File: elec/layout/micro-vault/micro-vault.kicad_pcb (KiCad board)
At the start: 2 copper layers, 2 parts

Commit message: layout complete
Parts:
- added C1: 100nF ±10% 16V X7R, atopile:C0402-b3ef17, F.Cu at (111.5, 89.5)
- added C2: 10µF ±10% 10V X5R, atopile:C0603-bd72f6, F.Cu at (114.7, 95.0)
- added C3: 100nF ±10% 16V X7R, atopile:C0402-b3ef17, F.Cu at (107.9, 94.6)
- added C4: 1µF ±10% 25V X5R, atopile:C0402-b3ef17, F.Cu at (116.4, 94.8)
- added C5: 1µF ±10% 25V X5R, atopile:C0402-b3ef17, F.Cu at (124.0, 93.5)
- added C6: 10µF ±10% 10V X5R, atopile:C0603-bd72f6, F.Cu at (124.2, 94.8)
- added C7: 10µF ±10% 10V X5R, atopile:C0603-bd72f6, F.Cu at (124.2, 96.2)
- added C8: 1µF ±10% 25V X5R, atopile:C0402-b3ef17, F.Cu at (113.5, 108.1)
- added C9: 1µF ±10% 25V X5R, atopile:C0402-b3ef17, F.Cu at (109.1, 108.1)
- added Q1: , atopile:SOT-23-3_L2.9-W1.6-P1.90-LS2.8-BR-186170, F.Cu at (123.9, 100.1)
- added R1: 1MΩ ±1% 62.5mW, atopile:R0402-56259e, F.Cu at (119.1, 107.0)
- added R10: 3kΩ ±0% 62.5mW, atopile:R0402-56259e, F.Cu at (112.3, 105.8)
- added R11: 10kΩ ±1% 62.5mW, atopile:R0402-56259e, F.Cu at (110.3, 105.8)
- added R12: 22Ω ±1% 100mW, atopile:R0603-ebcab9, F.Cu at (120.0, 90.2)
- added R13: 22Ω ±1% 100mW, atopile:R0603-ebcab9, F.Cu at (115.6, 92.0)
- added R14: 22Ω ±1% 100mW, atopile:R0603-ebcab9, F.Cu at (107.6, 91.7)
- added R15: 22Ω ±1% 100mW, atopile:R0603-ebcab9, F.Cu at (111.3, 100.4)
- added R2: 22Ω ±1% 100mW, atopile:R0603-ebcab9, F.Cu at (115.7, 97.5)
- added R3: 22Ω ±1% 100mW, atopile:R0603-ebcab9, F.Cu at (119.9, 99.4)
- added R4: 22Ω ±1% 100mW, atopile:R0603-ebcab9, F.Cu at (123.9, 97.8)
- added R5: 22Ω ±1% 100mW, atopile:R0603-ebcab9, F.Cu at (123.6, 92.2)
- added R6: 10kΩ ±1% 62.5mW, atopile:R0402-56259e, F.Cu at (126.5, 100.3)
- added R7: 10kΩ ±1% 62.5mW, atopile:R0402-56259e, F.Cu at (126.5, 98.2)
- added R8: 12kΩ ±1% 62.5mW, atopile:R0402-56259e, F.Cu at (122.6, 109.7)
- added R9: 88.7kΩ ±0% 62.5mW, atopile:R0402-56259e, F.Cu at (120.6, 109.7)
- added U3: , atopile:TSSOP-16_L5.0-W4.4-P0.65-LS6.4-BL-4f6acc, F.Cu at (111.2, 94.6)
- added U5: , atopile:VSSOP-8_L3.0-W3.0-P0.65-LS4.9-BL-beff67, F.Cu at (122.7, 107.4)
- added U6: , atopile:SOIC-8_L5.0-W4.0-P1.27-LS6.0-BL-294f77, F.Cu at (119.8, 94.7)
- added U7: , lib:SOT-23-5_L3.0-W1.7-P0.95-LS2.8-BL, F.Cu at (111.2, 108.3)
- added U8: , atopile:WSON-6_L2.0-W2.0-P0.65-TL-EP-c93430, F.Cu at (115.5, 99.9)
- U1: footprint atopile:TSSOP-16_L5.0-W4.4-P0.65-LS6.4-BL-4f6acc -> lib:NetTie-2_SMD_Pad0.25mm
- U2: footprint atopile:SOIC-8_L5.0-W4.0-P1.27-LS6.0-BL-294f77 -> lib:NetTie-2_SMD_Pad0.25mm
- moved U2 151.9 mm to (111.6, 93.0), turned to 180 degrees
- moved U1 146.4 mm to (110.5, 96.0)
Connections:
- U1 pad 1: A0 -> gnd
- U1 pad 2: A1 -> gnd-1
- U2 pad 1: DNC -> hv-2
- U2 pad 2: VIN -> hv-1
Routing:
- net gnd: track 0.00 -> 91.3 mm, vias 0 -> 7
- net hv-1: track 0.00 -> 51.8 mm, vias 0 -> 6
- net SCL: track 0.00 -> 21.2 mm, vias 0 -> 2
- net hv-3: track 0.00 -> 20.5 mm, vias 0 -> 2
- net SDA: track 0.00 -> 19.5 mm, vias 0 -> 2
- net Vplus: track 0.00 -> 17.5 mm, vias 0 -> 2
- net OUT1: track 0.00 -> 16.8 mm
- net TEMP: track 0.00 -> 16.5 mm, vias 0 -> 2
- net gnd-1: track 0.00 -> 15.1 mm, vias 0 -> 3
- net heater_controller-gnd: track 0.00 -> 12.6 mm, vias 0 -> 2
- net heater_controller-net-5: track 0.00 -> 10.5 mm, vias 0 -> 2
- net heater_controller-net-6: track 0.00 -> 9.44 mm
- net hv-2: track 0.00 -> 7.33 mm, vias 0 -> 2
- net heater_controller-net-4: track 0.00 -> 7.27 mm
- net hv: track 0.00 -> 7.05 mm
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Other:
- board outline added: 28 x 20 mm

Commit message: add logo
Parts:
- R10: value 3kΩ ±0% 62.5mW -> 10kΩ ±1% 62.5mW
- R11: value 10kΩ ±1% 62.5mW -> 36kΩ ±1% 62.5mW
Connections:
- C3 pad 1: hv-1 -> hv-3
- C4 pad 1: hv-1 -> hv-3
- C8 pad 1: hv-3 -> hv-1
- C9 pad 1: hv-1 -> hv-3
- R11 pad 1: hv-1 -> hv-3
- R12 pad 1: heater_controller-net-3 -> heater_controller-net-1
- R12 pad 2: heater_controller-net-1 -> heater_controller-net
- R13 pad 1: heater_controller-net-1 -> heater_controller-net
- R13 pad 2: heater_controller-net-5 -> heater_controller-net-4
- R14 pad 1: heater_controller-net-5 -> heater_controller-net-4
- R14 pad 2: heater_controller-net-6 -> heater_controller-net-2
- R15 pad 1: heater_controller-net-6 -> heater_controller-net-2
- R2 pad 1: hv-3 -> hv-1
- R2 pad 2: heater_controller-net -> heater_controller-net-3
- R3 pad 1: heater_controller-net -> heater_controller-net-3
- R3 pad 2: heater_controller-net-2 -> heater_controller-net-6
- R4 pad 1: heater_controller-net-2 -> heater_controller-net-6
- R4 pad 2: heater_controller-net-4 -> heater_controller-net-5
- R5 pad 1: heater_controller-net-4 -> heater_controller-net-5
- R5 pad 2: heater_controller-net-3 -> heater_controller-net-1
- R9 pad 1: hv-1 -> hv-3
- U2 pad 2: hv-1 -> hv-3
- U3 pad 13: hv-1 -> hv-3
- U3 pad 3: hv-1 -> hv-3
- U6 pad 2: hv-1 -> hv-3
- U7 pad 1: hv-3 -> hv-1
- U7 pad 3: hv-3 -> hv-1
- U7 pad 5: hv-1 -> hv-3
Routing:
- net hv-3: track 20.5 -> 51.8 mm, vias 2 -> 6
- net hv-1: track 51.8 -> 20.5 mm, vias 6 -> 2
- net heater_controller-net-6: track 9.44 -> 2.93 mm
- net heater_controller-net-2: track 2.93 -> 9.44 mm
- net heater_controller-net-5: track 10.5 -> 7.27 mm, vias 2 -> 0
- net heater_controller-net-4: track 7.27 -> 10.5 mm, vias 0 -> 2

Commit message: update layout
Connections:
- net TEMP renamed IN1minus
- C3 pad 1: hv-3 -> hv-1
- C4 pad 1: hv-3 -> hv-1
- C8 pad 1: hv-1 -> hv-3
- C9 pad 1: hv-3 -> hv-1
- R11 pad 1: hv-3 -> hv-1
- R12 pad 1: heater_controller-net-1 -> heater_controller-net-5
- R13 pad 2: heater_controller-net-4 -> heater_controller-net-1
- R14 pad 1: heater_controller-net-4 -> heater_controller-net-1
- R14 pad 2: heater_controller-net-2 -> heater_controller-net-4
- R15 pad 1: heater_controller-net-2 -> heater_controller-net-4
- R2 pad 1: hv-1 -> hv-3
- R2 pad 2: heater_controller-net-3 -> heater_controller-net-2
- R3 pad 1: heater_controller-net-3 -> heater_controller-net-2
- R4 pad 2: heater_controller-net-5 -> heater_controller-net-3
- R5 pad 1: heater_controller-net-5 -> heater_controller-net-3
- R5 pad 2: heater_controller-net-1 -> heater_controller-net-5
- R9 pad 1: hv-3 -> hv-1
- U2 pad 2: hv-3 -> hv-1
- U3 pad 13: hv-3 -> hv-1
- U3 pad 3: hv-3 -> hv-1
- U6 pad 2: hv-3 -> hv-1
- U7 pad 1: hv-1 -> hv-3
- U7 pad 3: hv-1 -> hv-3
- U7 pad 5: hv-3 -> hv-1
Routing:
- net hv-3: track 51.8 -> 20.5 mm, vias 6 -> 2
- net hv-1: track 20.5 -> 51.8 mm, vias 2 -> 6
- net heater_controller-net-1: track 3.89 -> 10.5 mm, vias 0 -> 2
- net heater_controller-net-2: track 9.44 -> 3.53 mm
- net heater_controller-net-3: track 3.53 -> 7.27 mm
- net heater_controller-net-5: track 7.27 -> 3.89 mm
- net heater_controller-net-4: track 10.5 -> 9.44 mm, vias 2 -> 0
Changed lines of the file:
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@@
 	(net 4 "IN2minus")
 	(net 5 "hv-2")
-	(net 6 "heater_controller-net-3")
+	(net 6 "heater_controller-net-2")
 	(net 7 "gnd")
 	(net 8 "reference.ic.footprint.pins[6].net-net")
@@
 	(net 17 "TRIMNR")
 	(net 18 "ADJ_NC")
-	(net 19 "heater_controller-net-5")
+	(net 19 "heater_controller-net-3")
 	(net 20 "AIN1")
 	(net 21 "IN2plus")
-	(net 22 "hv-3")
+	(net 22 "hv-1")
 	(net 23 "heater_controller-net-6")
 	(net 24 "REFN")
 	(net 25 "SCL")
-	(net 26 "TEMP")
-	(net 27 "hv-1")
+	(net 26 "IN1minus")
+	(net 27 "hv-3")
 	(net 28 "IN1plus")
 	(net 29 "gate")
 	(net 30 "heater_controller-gnd")
-	(net 31 "heater_controller-net-4")
-	(net 32 "heater_controller-net-2")
-	(net 33 "heater_controller-net-1")
+	(net 31 "heater_controller-net-1")
+	(net 32 "heater_controller-net-4")
+	(net 33 "heater_controller-net-5")
 	(net 34 "heater_controller-net")
 	(net 35 "OUT1")
@@
 			(size 0.81 0.86)
 			(layers "F.Cu" "F.Mask" "F.Paste")
-			(net 31 "heater_controller-net-4")
+			(net 31 "heater_controller-net-1")
 		)
 		(embedded_fonts no)
@@
 			(size 0.79 0.54)
 			(layers "F.Cu" "F.Mask" "F.Paste")
-			(net 22 "hv-3")
+			(net 22 "hv-1")
 		)
 		(pad "2" smd rect
@@
 			(size 0.81 0.86)
 			(layers "F.Cu" "F.Mask" "F.Paste")
-			(net 27 "hv-1")
+			(net 27 "hv-3")
 		)
 		(pad "2" smd rect
@@
 			(size 0.81 0.86)
 			(layers "F.Cu" "F.Mask" "F.Paste")
-			(net 6 "heater_controller-net-3")
+			(net 6 "heater_controller-net-2")
 		)
 		(embedded_fonts no)
@@
 			(size 0.81 0.86)
 			(layers "F.Cu" "F.Mask" "F.Paste")
-			(net 19 "heater_controller-net-5")
+			(net 19 "heater_controller-net-3")
 		)
 		(pad "2" smd rect
@@
 			(size 0.81 0.86)
 			(layers "F.Cu" "F.Mask" "F.Paste")
-			(net 33 "heater_controller-net-1")
+			(net 33 "heater_controller-net-5")
 		)
 		(embedded_fonts no)
@@
 			(size 0.25 0.25)
 			(layers "F.Cu")
-			(net 22 "hv-3")
+			(net 22 "hv-1")
 		)
 		(embedded_fonts no)
@@
 			(size 0.57 0.54)
 			(layers "F.Cu" "F.Mask" "F.Paste")
-			(net 22 "hv-3")
+			(net 22 "hv-1")
 		)
 		(pad "2" smd rect
@@
 			(size 0.79 0.54)
 			(layers "F.Cu" "F.Mask" "F.Paste")
-			(net 22 "hv-3")
+			(net 22 "hv-1")
 		)
 		(pad "2" smd rect
@@
 			(size 0.81 0.86)
 			(layers "F.Cu" "F.Mask" "F.Paste")
-			(net 32 "heater_controller-net-2")
+			(net 32 "heater_controller-net-4")
 		)
 		(pad "2" smd rect
@@
 			(size 0.79 0.54)
 			(layers "F.Cu" "F.Mask" "F.Paste")
-			(net 27 "hv-1")
+			(net 27 "hv-3")
 		)
 		(pad "2" smd rect
@@
 			(size 0.81 0.86)
 			(layers "F.Cu" "F.Mask" "F.Paste")
-			(net 6 "heater_controller-net-3")
+			(net 6 "heater_controller-net-2")
 		)
 		(pad "2" smd rect
@@
 			(size 0.57 0.54)
 			(layers "F.Cu" "F.Mask" "F.Paste")
-			(net 22 "hv-3")
+			(net 22 "hv-1")
 		)
 		(pad "2" smd rect
@@
 			(size 0.81 0.86)
 			(layers "F.Cu" "F.Mask" "F.Paste")
-			(net 33 "heater_controller-net-1")
+			(net 33 "heater_controller-net-5")
 		)
 		(pad "2" smd rect
@@
 			(size 0.81 0.86)
 			(layers "F.Cu" "F.Mask" "F.Paste")
-			(net 19 "heater_controller-net-5")
+			(net 19 "heater_controller-net-3")
 		)
 		(embedded_fonts no)
@@
 			(size 0.57 1.95)
 			(layers "F.Cu" "F.Mask" "F.Paste")
-			(net 22 "hv-3")
+			(net 22 "hv-1")
 		)
 		(pad "3" smd oval
@@
 			(size 0.57 1.95)
 			(layers "F.Cu" "F.Mask" "F.Paste")
-			(net 26 "TEMP")
+			(net 26 "IN1minus")
 		)
 		(pad "4" smd oval
@@
 			(size 0.49 1.16)
 			(layers "F.Cu" "F.Mask" "F.Paste")
-			(net 27 "hv-1")
+			(net 27 "hv-3")
 		)
 		(pad "2" smd rect
@@
 			(size 0.49 1.16)
 			(layers "F.Cu" "F.Mask" "F.Paste")
-			(net 27 "hv-1")
+			(net 27 "hv-3")
 		)
 		(pad "4" smd rect
@@
 			(size 0.49 1.18)
 			(layers "F.Cu" "F.Mask" "F.Paste")
-			(net 22 "hv-3")
+			(net 22 "hv-1")
 		)
 		(embedded_fonts no)
@@
 			(size 0.79 0.54)
 			(layers "F.Cu" "F.Mask" "F.Paste")
-			(net 22 "hv-3")
+			(net 22 "hv-1")
 		)
 		(pad "2" smd rect
@@
 			(size 0.38 1.45)
 			(layers "F.Cu" "F.Mask" "F.Paste")
-			(net 26 "TEMP")
+			(net 26 "IN1minus")
 		)
 		(pad "3" smd oval
@@
 			(size 0.81 0.86)
 			(layers "F.Cu" "F.Mask" "F.Paste")
-			(net 31 "heater_controller-net-4")
+			(net 31 "heater_controller-net-1")
 		)
 		(pad "2" smd rect
@@
 			(size 0.81 0.86)
 			(layers "F.Cu" "F.Mask" "F.Paste")
-			(net 32 "heater_controller-net-2")
+			(net 32 "heater_controller-net-4")
 		)
 		(embedded_fonts no)
@@
 			(size 0.34 1.73)
 			(layers "F.Cu" "F.Mask" "F.Paste")
-			(net 22 "hv-3")
+			(net 22 "hv-1")
 		)
 		(pad "4" smd oval
@@
 			(size 0.34 1.73)
 			(layers "F.Cu" "F.Mask" "F.Paste")
-			(net 22 "hv-3")
+			(net 22 "hv-1")
 		)
 		(pad "14" smd oval

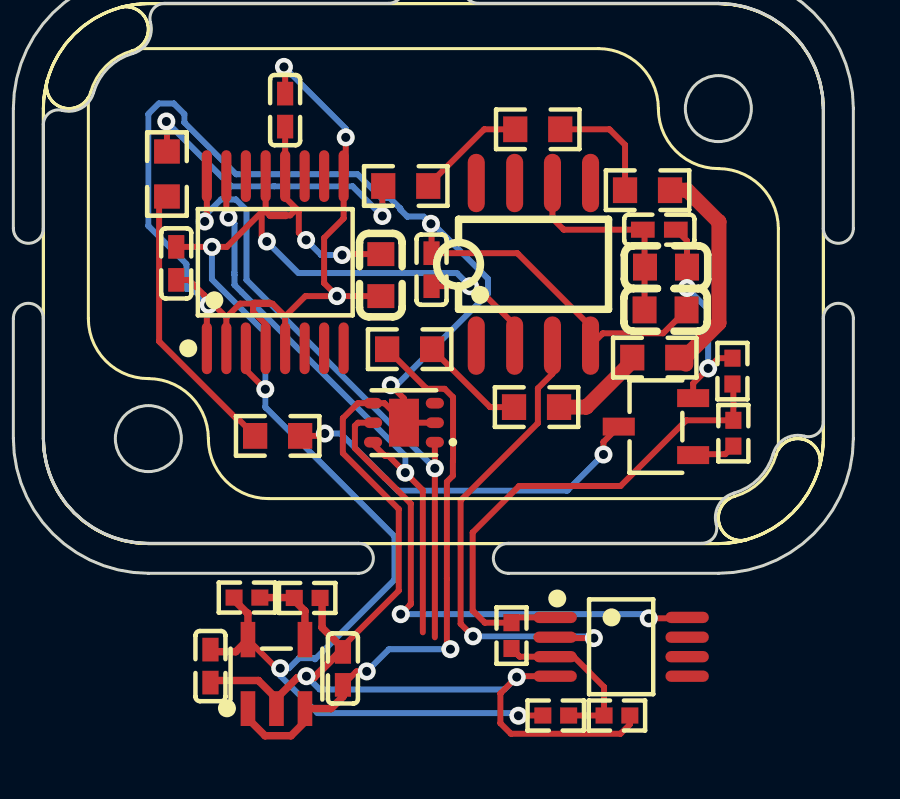
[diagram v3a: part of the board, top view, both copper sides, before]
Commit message: attach reference input to ADC
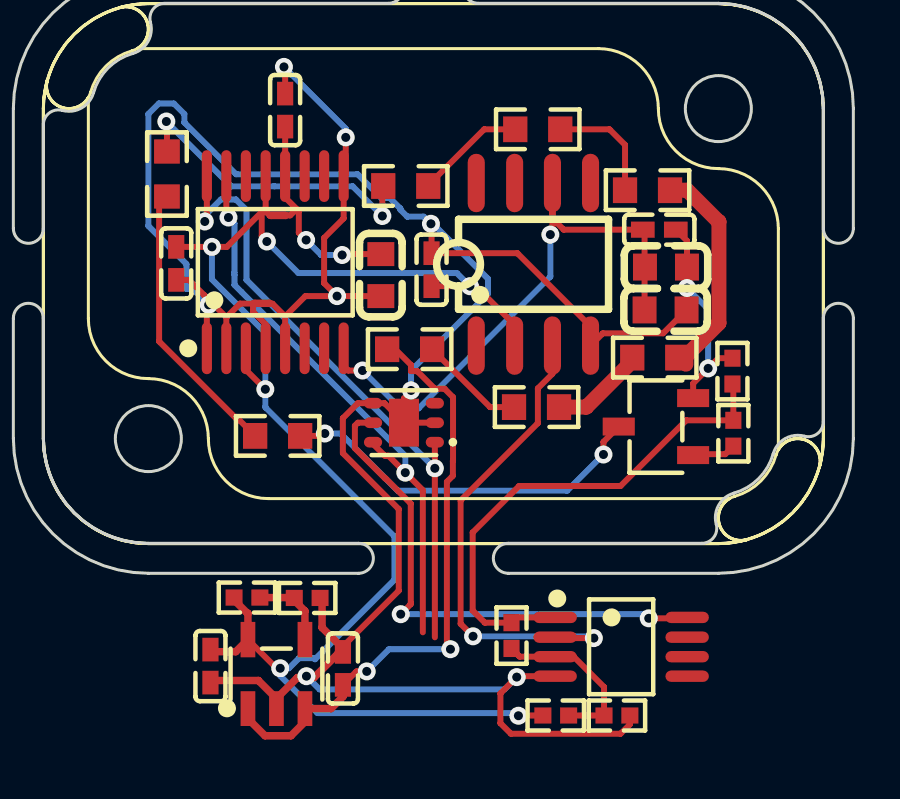
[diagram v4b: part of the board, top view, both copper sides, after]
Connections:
- C1 pad 2: gnd-1 -> gnd
- C2 pad 2: gnd-1 -> gnd
- C3 pad 1: hv-1 -> hv
- C4 pad 1: hv-1 -> hv
- C5 pad 1: hv -> hv-3
- C6 pad 1: hv -> hv-3
- C7 pad 1: hv -> hv-3
- C8 pad 1: hv-3 -> hv-1
- C9 pad 1: hv-1 -> hv
- R11 pad 1: hv-1 -> hv
- R12 pad 1: heater_controller-net-5 -> heater_controller-net-6
- R12 pad 2: heater_controller-net -> heater_controller-net-2
- R13 pad 1: heater_controller-net -> heater_controller-net-2
- R13 pad 2: heater_controller-net-1 -> heater_controller-net-4
- R14 pad 1: heater_controller-net-1 -> heater_controller-net-4
- R14 pad 2: heater_controller-net-4 -> heater_controller-net-5
- R15 pad 1: heater_controller-net-4 -> heater_controller-net-5
- R2 pad 1: hv-3 -> hv-1
- R2 pad 2: heater_controller-net-2 -> heater_controller-net
- R3 pad 1: heater_controller-net-2 -> heater_controller-net
- R3 pad 2: heater_controller-net-6 -> heater_controller-net-1
- R4 pad 1: heater_controller-net-6 -> heater_controller-net-1
- R5 pad 2: heater_controller-net-5 -> heater_controller-net-6
- R9 pad 1: hv-1 -> hv
- U1 pad 2: gnd-1 -> gnd
- U2 pad 2: hv-1 -> hv
- U3 pad 13: hv-1 -> hv
- U3 pad 3: hv-1 -> hv
- U3 pad 5: gnd-1 -> gnd
- U3 pad 8: REFN -> hv-3
- U3 pad 9: gnd-1 -> gnd
- U6 pad 2: hv-1 -> hv
- U6 pad 6: hv -> hv-3
- U7 pad 1: hv-3 -> hv-1
- U7 pad 3: hv-3 -> hv-1
- U7 pad 5: hv-1 -> hv
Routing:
- net hv: track 7.05 -> 51.8 mm, vias 0 -> 6
- net hv-1: track 51.8 -> 20.6 mm, vias 6 -> 2
- net gnd-1: track 15.1 -> 0.00 mm, vias 3 -> 0
- net gnd: track 91.3 -> 105.9 mm, vias 7 -> 10
- net heater_controller-net-1: track 10.5 -> 2.93 mm, vias 2 -> 0
- net heater_controller-net-5: track 3.89 -> 9.44 mm
- net heater_controller-net-4: track 9.44 -> 10.5 mm, vias 0 -> 2
- net heater_controller-net-6: track 2.93 -> 3.89 mm

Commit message: increase uVault heater power ~30%
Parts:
- R12, R13, R14, R15, R2, R3, R4, R5: value 22Ω ±1% 100mW -> 15Ω ±1% 100mW
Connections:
- net IN1minus renamed TEMP
- C1 pad 1: hv-2 -> hv-1
- C2 pad 1: hv-2 -> hv-1
- C3 pad 1: hv -> hv-2
- C4 pad 1: hv -> hv-2
- C8 pad 1: hv-1 -> hv
- C9 pad 1: hv -> hv-2
- R11 pad 1: hv -> hv-2
- R12 pad 1: heater_controller-net-6 -> heater_controller-net-4
- R12 pad 2: heater_controller-net-2 -> heater_controller-net-3
- R13 pad 1: heater_controller-net-2 -> heater_controller-net-3
- R13 pad 2: heater_controller-net-4 -> heater_controller-net
- R14 pad 1: heater_controller-net-4 -> heater_controller-net
- R2 pad 1: hv-1 -> hv
- R2 pad 2: heater_controller-net -> heater_controller-net-2
- R3 pad 1: heater_controller-net -> heater_controller-net-2
- R4 pad 2: heater_controller-net-3 -> heater_controller-net-6
- R5 pad 1: heater_controller-net-3 -> heater_controller-net-6
- R5 pad 2: heater_controller-net-6 -> heater_controller-net-4
- R9 pad 1: hv -> hv-2
- U2 pad 1: hv-2 -> hv-1
- U2 pad 2: hv -> hv-2
- U3 pad 12: hv-2 -> hv-1
- U3 pad 13: hv -> hv-2
- U3 pad 3: hv -> hv-2
- U6 pad 2: hv -> hv-2
- U7 pad 1: hv-1 -> hv
- U7 pad 3: hv-1 -> hv
- U7 pad 5: hv -> hv-2
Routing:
- net hv-2: track 7.33 -> 51.8 mm, vias 2 -> 6
- net hv: track 51.8 -> 20.6 mm, vias 6 -> 2
- net hv-1: track 20.6 -> 7.33 mm
- net heater_controller-net: track 3.53 -> 10.5 mm, vias 0 -> 2
- net heater_controller-net-4: track 10.5 -> 3.89 mm, vias 2 -> 0
- net heater_controller-net-3: track 7.27 -> 3.70 mm
- net heater_controller-net-6: track 3.89 -> 7.27 mm

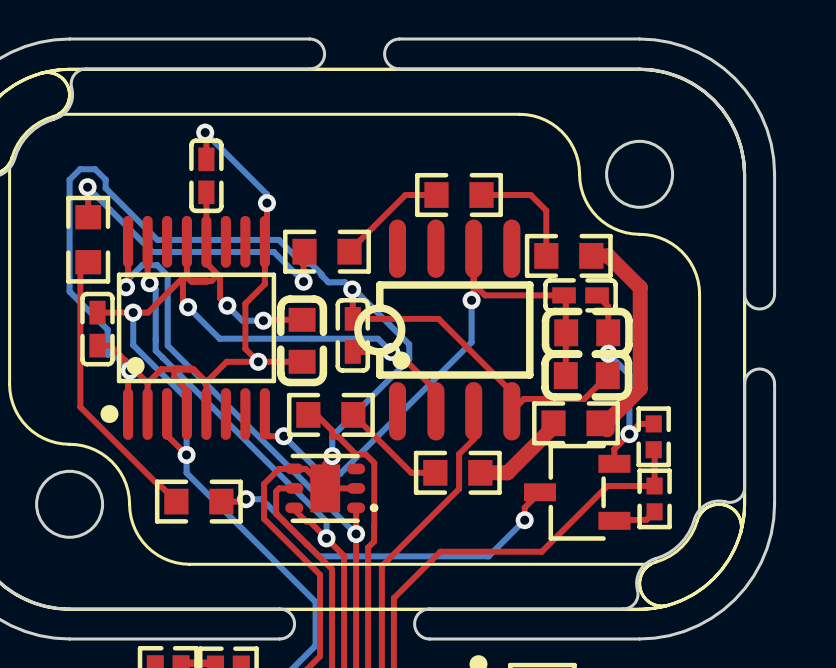
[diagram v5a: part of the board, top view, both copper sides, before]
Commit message: remove vendored tca9548a, make thermistor 8ch block, make saleae debug header layout
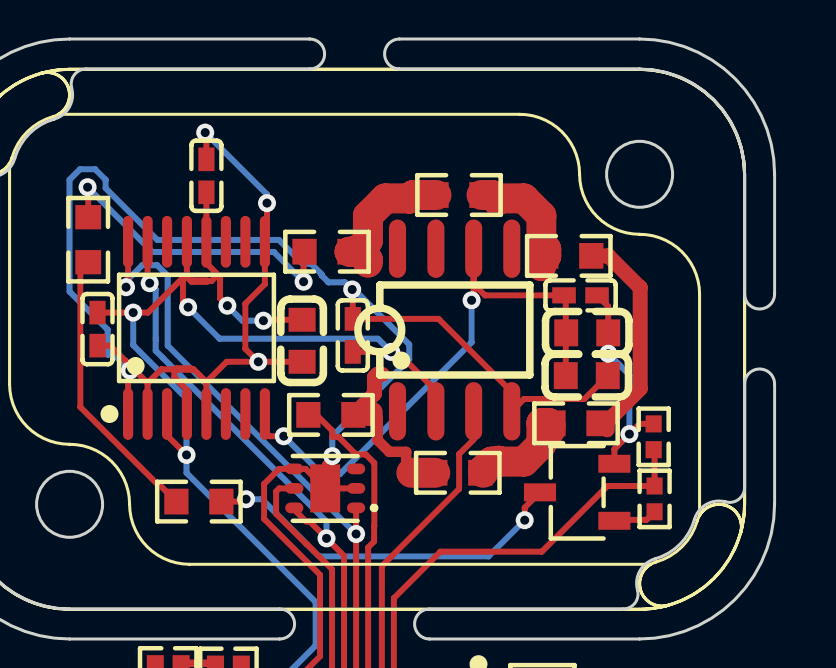
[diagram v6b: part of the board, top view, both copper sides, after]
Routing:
- net heater_controller-net-2: track 3.53 -> 6.47 mm
- net heater_controller-net-3: track 3.70 -> 4.99 mm
- net heater_controller-net-1: track 2.93 -> 3.62 mm

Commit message: building frozen
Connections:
- net TEMP renamed IN1minus
- C1 pad 1: hv-1 -> hv-3
- C2 pad 1: hv-1 -> hv-3
- C3 pad 1: hv-2 -> hv-1
- C4 pad 1: hv-2 -> hv-1
- C5 pad 1: hv-3 -> hv-2
- C6 pad 1: hv-3 -> hv-2
- C7 pad 1: hv-3 -> hv-2
- C9 pad 1: hv-2 -> hv-1
- R11 pad 1: hv-2 -> hv-1
- R12 pad 1: heater_controller-net-4 -> heater_controller-net
- R12 pad 2: heater_controller-net-3 -> heater_controller-net-4
- R13 pad 1: heater_controller-net-3 -> heater_controller-net-4
- R13 pad 2: heater_controller-net -> heater_controller-net-1
- R14 pad 1: heater_controller-net -> heater_controller-net-1
- R14 pad 2: heater_controller-net-5 -> heater_controller-net-6
- R15 pad 1: heater_controller-net-5 -> heater_controller-net-6
- R3 pad 2: heater_controller-net-1 -> heater_controller-net-3
- R4 pad 1: heater_controller-net-1 -> heater_controller-net-3
- R4 pad 2: heater_controller-net-6 -> heater_controller-net-5
- R5 pad 1: heater_controller-net-6 -> heater_controller-net-5
- R5 pad 2: heater_controller-net-4 -> heater_controller-net
- R9 pad 1: hv-2 -> hv-1
- U2 pad 1: hv-1 -> hv-3
- U2 pad 2: hv-2 -> hv-1
- U3 pad 12: hv-1 -> hv-3
- U3 pad 13: hv-2 -> hv-1
- U3 pad 3: hv-2 -> hv-1
- U3 pad 8: hv-3 -> hv-2
- U6 pad 2: hv-2 -> hv-1
- U6 pad 6: hv-3 -> hv-2
- U7 pad 5: hv-2 -> hv-1
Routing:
- net hv-1: track 7.33 -> 51.8 mm, vias 2 -> 6
- net hv-2: track 51.8 -> 20.1 mm, vias 6 -> 2
- net hv-3: track 20.1 -> 7.33 mm
- net heater_controller-net-1: track 3.62 -> 10.5 mm, vias 0 -> 2
- net heater_controller-net: track 10.5 -> 4.25 mm, vias 2 -> 0
- net heater_controller-net-6: track 7.27 -> 9.44 mm
- net heater_controller-net-5: track 9.44 -> 7.27 mm
- net heater_controller-net-3: track 4.99 -> 3.62 mm
- net heater_controller-net-4: track 4.25 -> 4.99 mm
